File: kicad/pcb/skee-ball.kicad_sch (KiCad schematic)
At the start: 37 parts, among them J1 SPEAKER_P, J10 NHD_RW, J11 NHD_DB1, J12 NHD_DB0, J13 US_ECHO0, J14 US_ECHO1, J15 US_ECHO2, J16 US_ECHO3, J17 US_ECHO4, J18 US_TRIG0, J19 US_TRIG1, J2 SPEAKER_N, J20 US_TRIG2, J21 US_TRIG3, J22 US_TRIG4, J23 NHD_E2, J24 NHD_E2, J25 ADC_IN1, J26 PWM_SERVO_6, J27 PWM_DC (TIM17_CH1), J28 BUTTON, J29 NHD_V0, J3 NHD_DB7, J4 NHD_DB6, J5 NHD_DB5, J6 NHD_DB4, J7 NHD_DB3, J8 NHD_DB2, J9 NHD_RS, U1 D24V22F6, U2 MAX98357A, U3 D24V22F5, U4 STM32F091RCTx, U5 74HC595, U6 74HC595, U7 74LS08

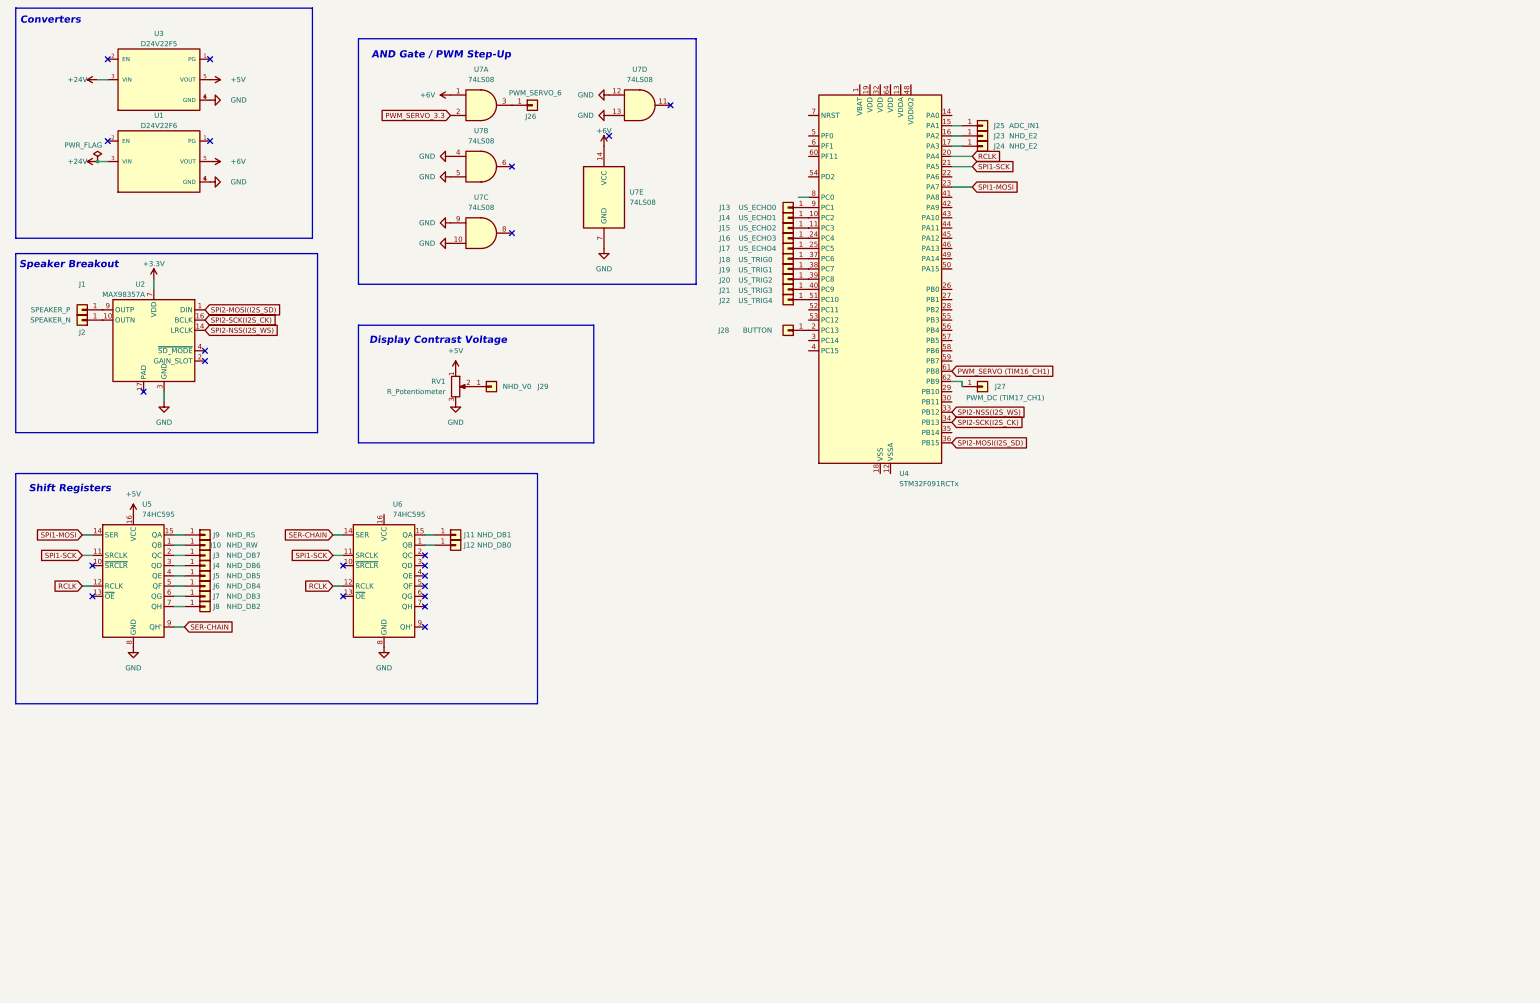
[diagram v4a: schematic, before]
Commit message: add LDOs to pcb schematic
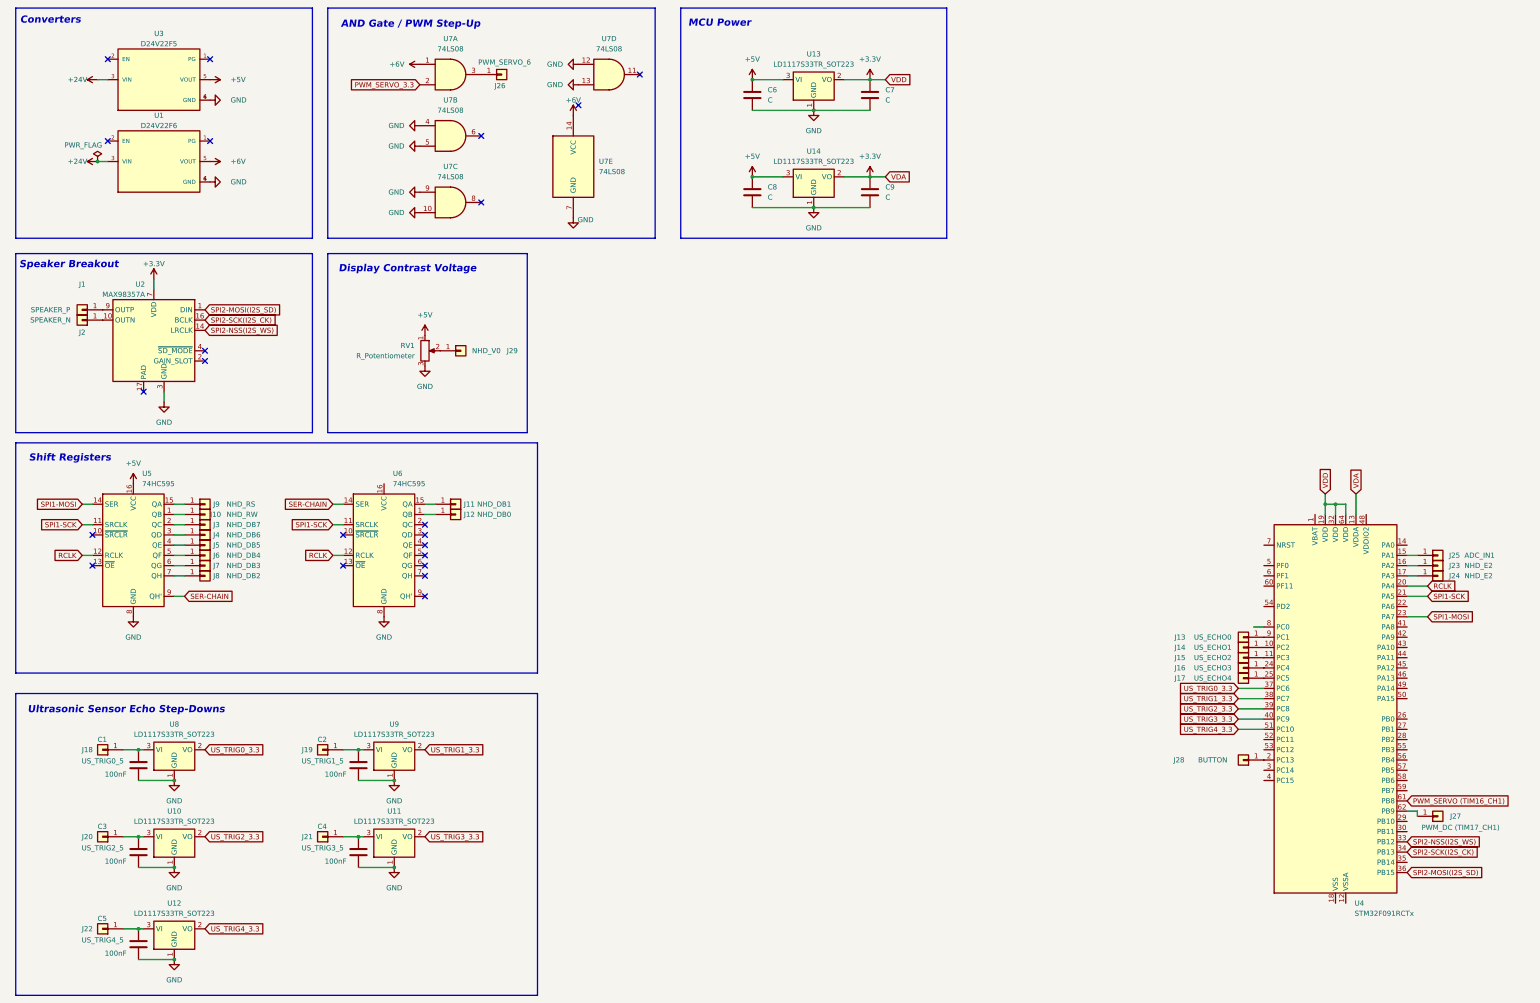
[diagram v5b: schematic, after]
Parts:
- added C1, C2, C3, C4, C5: 100nF, symbol Device:C
- added C6, C7, C8, C9: C, symbol Device:C
- added U10, U11, U12, U13, U14, U8, U9: LD1117S33TR_SOT223, Package_TO_SOT_SMD:SOT-223-3_TabPin2, symbol Regulator_Linear:LD1117S33TR_SOT223
- J18: value US_TRIG0 -> US_TRIG0_5
- J19: value US_TRIG1 -> US_TRIG1_5
- J20: value US_TRIG2 -> US_TRIG2_5
- J21: value US_TRIG3 -> US_TRIG3_5
- J22: value US_TRIG4 -> US_TRIG4_5
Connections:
- net +3.3V: now also U4.13 (VDDA), U4.19 (VDD), U4.32 (VDD), U4.64 (VDD), C7.1, C9.1, U13.2 (VO), U14.2 (VO)
- net +5V: now also C6.1, C8.1, U13.3 (VI), U14.3 (VI)
- net GND: now also C1.2, C2.2, C3.2, C4.2, C5.2, C6.2, C7.2, C8.2, C9.2, U10.1 (GND), U11.1 (GND), U12.1 (GND), U13.1 (GND), U14.1 (GND), U8.1 (GND), U9.1 (GND)
- net at J19.1 (Pin_1): now also C2.1, U9.3 (VI); no longer U4.38 (PC7)
- net at J21.1 (Pin_1): now also C4.1, U11.3 (VI); no longer U4.40 (PC9)
- net at J20.1 (Pin_1): now also C3.1, U10.3 (VI); no longer U4.39 (PC8)
- net at J18.1 (Pin_1): now also C1.1, U8.3 (VI); no longer U4.37 (PC6)
- net at J22.1 (Pin_1): now also C5.1, U12.3 (VI); no longer U4.51 (PC10)
- new net US_TRIG0_3.3: U4.37 (PC6), U8.2 (VO)
- new net US_TRIG1_3.3: U4.38 (PC7), U9.2 (VO)
- new net US_TRIG2_3.3: U10.2 (VO), U4.39 (PC8)
- new net US_TRIG3_3.3: U11.2 (VO), U4.40 (PC9)
- new net US_TRIG4_3.3: U12.2 (VO), U4.51 (PC10)
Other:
- note added: "MCU Power"
- note added: "Ultrasonic Sensor Echo Step-Downs"
- moved on the sheet: J10, J11, J12, J13, J14, J15, J16, J17, J23, J24, J25, J26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

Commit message: update cap values for stm supply voltage
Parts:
- C6, C8: value C -> 100nF
- C7, C9: value C -> 10uF
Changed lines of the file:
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@@
 			)
 		)
-		(property "Value" "C"
+		(property "Value" "10uF"
 			(at 237.49 67.3099 0)
 			(effects
@@
 			)
 		)
-		(property "Value" "C"
+		(property "Value" "10uF"
 			(at 237.49 43.1799 0)
 			(effects
@@
 			)
 		)
-		(property "Value" "C"
+		(property "Value" "100nF"
 			(at 208.28 43.1799 0)
 			(effects
@@
 			)
 		)
-		(property "Value" "C"
+		(property "Value" "100nF"
 			(at 208.28 67.3099 0)
 			(effects

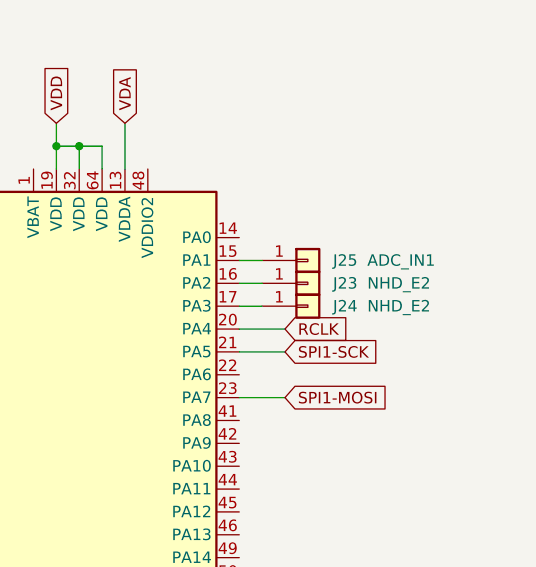
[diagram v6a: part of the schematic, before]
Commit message: fix nhd enable signal label on schematic
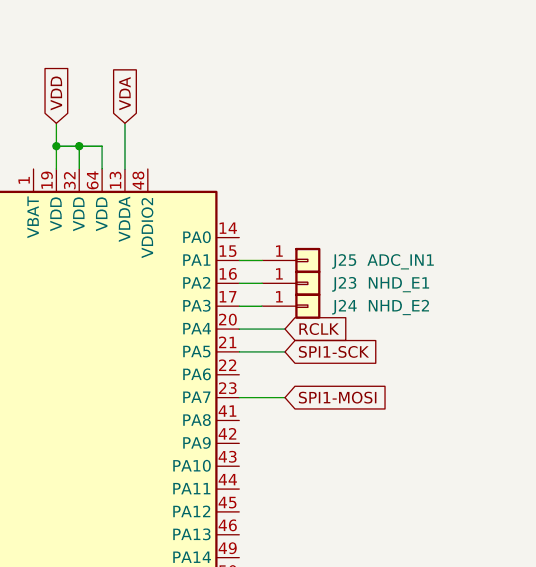
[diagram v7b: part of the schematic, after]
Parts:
- J23: value NHD_E2 -> NHD_E1
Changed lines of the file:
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@@
 			)
 		)
-		(property "Value" "NHD_E2"
+		(property "Value" "NHD_E1"
 			(at 381.254 158.75 0)
 			(effects
